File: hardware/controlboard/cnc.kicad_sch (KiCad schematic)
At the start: 31 parts, among them J1 Conn_02x04_Counter_Clockwise, J2 Conn_02x04_Row_Letter_Last, J5 Conn_02x04_Row_Letter_First, M1 Motor_Servo, Q1 NMOS AO3400A

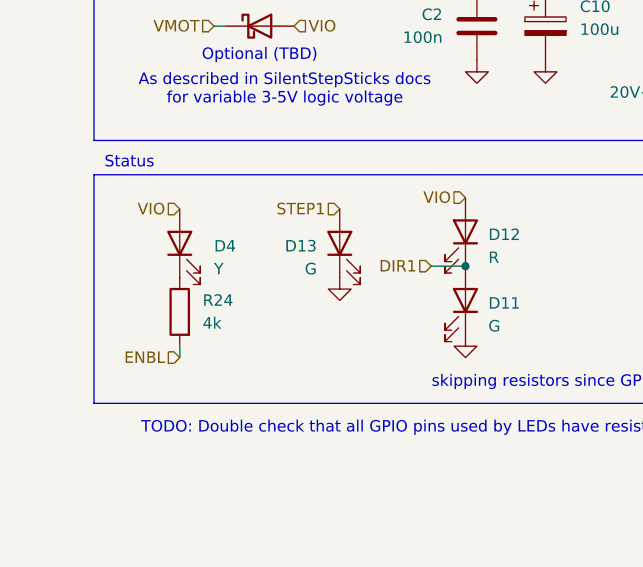
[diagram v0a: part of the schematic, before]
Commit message: Revert controlboard to June 12th 2024
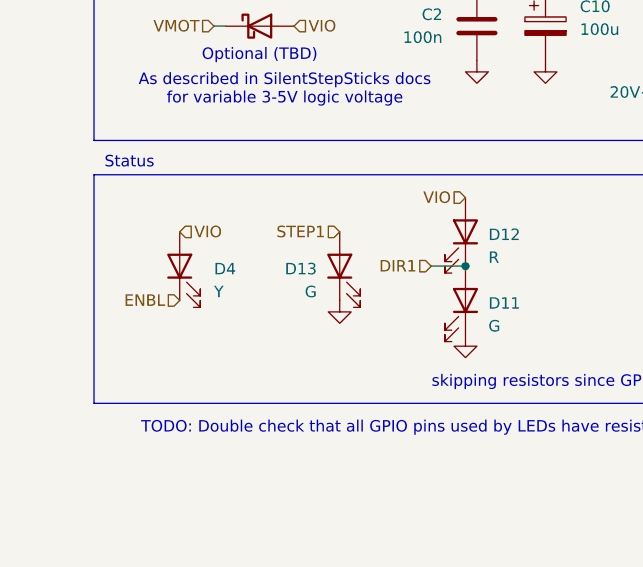
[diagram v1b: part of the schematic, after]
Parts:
- removed R24: 4k, Resistor_SMD:R_0603_1608Metric_Pad0.98x0.95mm_HandSolder, symbol Device:R
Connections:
- net ENBL: now also D4.1 (K)
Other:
- moved on the sheet: D13, D4
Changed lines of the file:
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@@
 	(wire
 		(pts
-			(xy 22.86 64.77) (xy 22.86 63.5)
-		)
-		(stroke
-			(width 0)
-			(type default)
-		)
-	)
-	(wire
-		(pts
 			(xy 234.95 57.15) (xy 234.95 58.42)
 		)
@@
 	(hierarchical_label "ENBL"
 		(shape input)
-		(at 22.86 64.77 180)
+		(at 22.86 58.42 180)
 		(fields_autoplaced yes)
 		(effects
@@
 	(hierarchical_label "STEP1"
 		(shape input)
-		(at 40.64 48.26 180)
+		(at 40.64 50.8 180)
 		(fields_autoplaced yes)
 		(effects
@@
 	(hierarchical_label "VIO"
 		(shape input)
-		(at 22.86 48.26 180)
+		(at 22.86 50.8 0)
 		(fields_autoplaced yes)
 		(effects
@@
 				(size 1.27 1.27)
 			)
-			(justify right)
+			(justify left)
 		)
 	)
@@
 	(symbol
 		(lib_id "power:GND")
-		(at 40.64 55.88 0)
+		(at 40.64 58.42 0)
 		(unit 1)
 		(exclude_from_sim no)
@@
 		(fields_autoplaced yes)
 		(property "Reference" "#PWR033"
-			(at 40.64 62.23 0)
+			(at 40.64 64.77 0)
 			(effects
 				(font
@@
 		)
 		(property "Value" "GND"
-			(at 40.64 60.96 0)
+			(at 40.64 63.5 0)
 			(effects
 				(font
@@
 		)
 		(property "Footprint" ""
-			(at 40.64 55.88 0)
+			(at 40.64 58.42 0)
 			(effects
 				(font
@@
 		)
 		(property "Datasheet" ""
-			(at 40.64 55.88 0)
+			(at 40.64 58.42 0)
 			(effects
 				(font
@@
 		)
 		(property "Description" "Power symbol creates a global label with name \"GND\" , ground"
-			(at 40.64 55.88 0)
+			(at 40.64 58.42 0)
 			(effects
 				(font
@@
 	(symbol
 		(lib_id "Device:LED")
-		(at 22.86 52.07 90)
+		(at 22.86 54.61 90)
 		(unit 1)
 		(exclude_from_sim no)
@@
 		(fields_autoplaced yes)
 		(property "Reference" "D4"
-			(at 26.67 52.3874 90)
+			(at 26.67 54.9274 90)
 			(effects
 				(font
@@
 		)
 		(property "Value" "Y"
-			(at 26.67 54.9274 90)
+			(at 26.67 57.4674 90)
 			(effects
 				(font
@@
 		)
 		(property "Footprint" "LED_SMD:LED_0603_1608Metric_Pad1.05x0.95mm_HandSolder"
-			(at 22.86 52.07 0)
+			(at 22.86 54.61 0)
 			(effects
 				(font
@@
 		)
 		(property "Datasheet" "~"
-			(at 22.86 52.07 0)
+			(at 22.86 54.61 0)
 			(effects
 				(font
@@
 		)
 		(property "Description" "Light emitting diode"
-			(at 22.86 52.07 0)
+			(at 22.86 54.61 0)
 			(effects
 				(font
@@
 		)
 		(property "JLCPCB Rotation Offset" ""
-			(at 22.86 52.07 0)
+			(at 22.86 54.61 0)
 			(effects
 				(font
@@
 	)
 	(symbol
-		(lib_id "Device:R")
-		(at 22.86 59.69 0)
-		(mirror y)
-		(unit 1)
-		(exclude_from_sim no)
-		(in_bom yes)
-		(on_board yes)
-		(dnp no)
-		(property "Reference" "R24"
-			(at 25.4 58.4199 0)
-			(effects
-				(font
-					(size 1.27 1.27)
-				)
-				(justify right)
-			)
-		)
-		(property "Value" "4k"
-			(at 25.4 60.9599 0)
-			(effects
-				(font
-					(size 1.27 1.27)
-				)
-				(justify right)
-			)
-		)
-		(property "Footprint" "Resistor_SMD:R_0603_1608Metric_Pad0.98x0.95mm_HandSolder"
-			(at 24.638 59.69 90)
-			(effects
-				(font
-					(size 1.27 1.27)
-				)
-				(hide yes)
-			)
-		)
-		(property "Datasheet" "~"
-			(at 22.86 59.69 0)
-			(effects
-				(font
-					(size 1.27 1.27)
-				)
-				(hide yes)
-			)
-		)
-		(property "Description" "Resistor"
-			(at 22.86 59.69 0)
-			(effects
-				(font
-					(size 1.27 1.27)
-				)
-				(hide yes)
-			)
-		)
-		(property "JLCPCB Rotation Offset" ""
-			(at 22.86 59.69 0)
-			(effects
-				(font
-					(size 1.27 1.27)
-				)
-				(hide yes)
-			)
-		)
-		(pin "2"
-		)
-		(pin "1"
-		)
-		(instances
-			(project "controlboard"
-				(path "/2797250d-6fee-4769-b4dd-0e20ce4f0941/5be4ea58-2822-4c96-82fa-ac7323f92cc7"
-					(reference "R24")
-					(unit 1)
-				)
-			)
-		)
-	)
-	(symbol
 		(lib_id "0chessbot-parts:Pololu_Breakout_MP6500")
 		(at 132.08 100.33 0)
@@
 	(symbol
 		(lib_id "Device:LED")
-		(at 40.64 52.07 90)
+		(at 40.64 54.61 90)
 		(unit 1)
 		(exclude_from_sim no)
@@
 		(dnp no)
 		(property "Reference" "D13"
-			(at 38.1 52.3874 90)
+			(at 38.1 54.9274 90)
 			(effects
 				(font
@@
 		)
 		(property "Value" "G"
-			(at 38.1 54.9274 90)
+			(at 38.1 57.4674 90)
 			(effects
 				(font
@@
 		)
 		(property "Footprint" "LED_SMD:LED_0603_1608Metric_Pad1.05x0.95mm_HandSolder"
-			(at 40.64 52.07 0)
+			(at 40.64 54.61 0)
 			(effects
 				(font
@@
 		)
 		(property "Datasheet" "~"
-			(at 40.64 52.07 0)
+			(at 40.64 54.61 0)
 			(effects
 				(font
@@
 		)
 		(property "Description" "Light emitting diode"
-			(at 40.64 52.07 0)
+			(at 40.64 54.61 0)
 			(effects
 				(font
@@
 		)
 		(property "JLCPCB Rotation Offset" ""
-			(at 40.64 52.07 0)
+			(at 40.64 54.61 0)
 			(effects
 				(font
